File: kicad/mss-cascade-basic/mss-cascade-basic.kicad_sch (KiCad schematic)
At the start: 94 parts, among them J1 Screw_Terminal_01x02, J10 Screw_Terminal_01x02, J2 SM04B-SRSS, J3 SM04B-SRSS, J4 SM04B-SRSS, J5 8P8C, J6 8P8C, J7 AVR-ISP, J8 Screw_Terminal_01x02, J9 Screw_Terminal_01x02, U1 AP7381-50Y, U2 ATtiny861A-S, U3 74HC4049, U4 AP3012

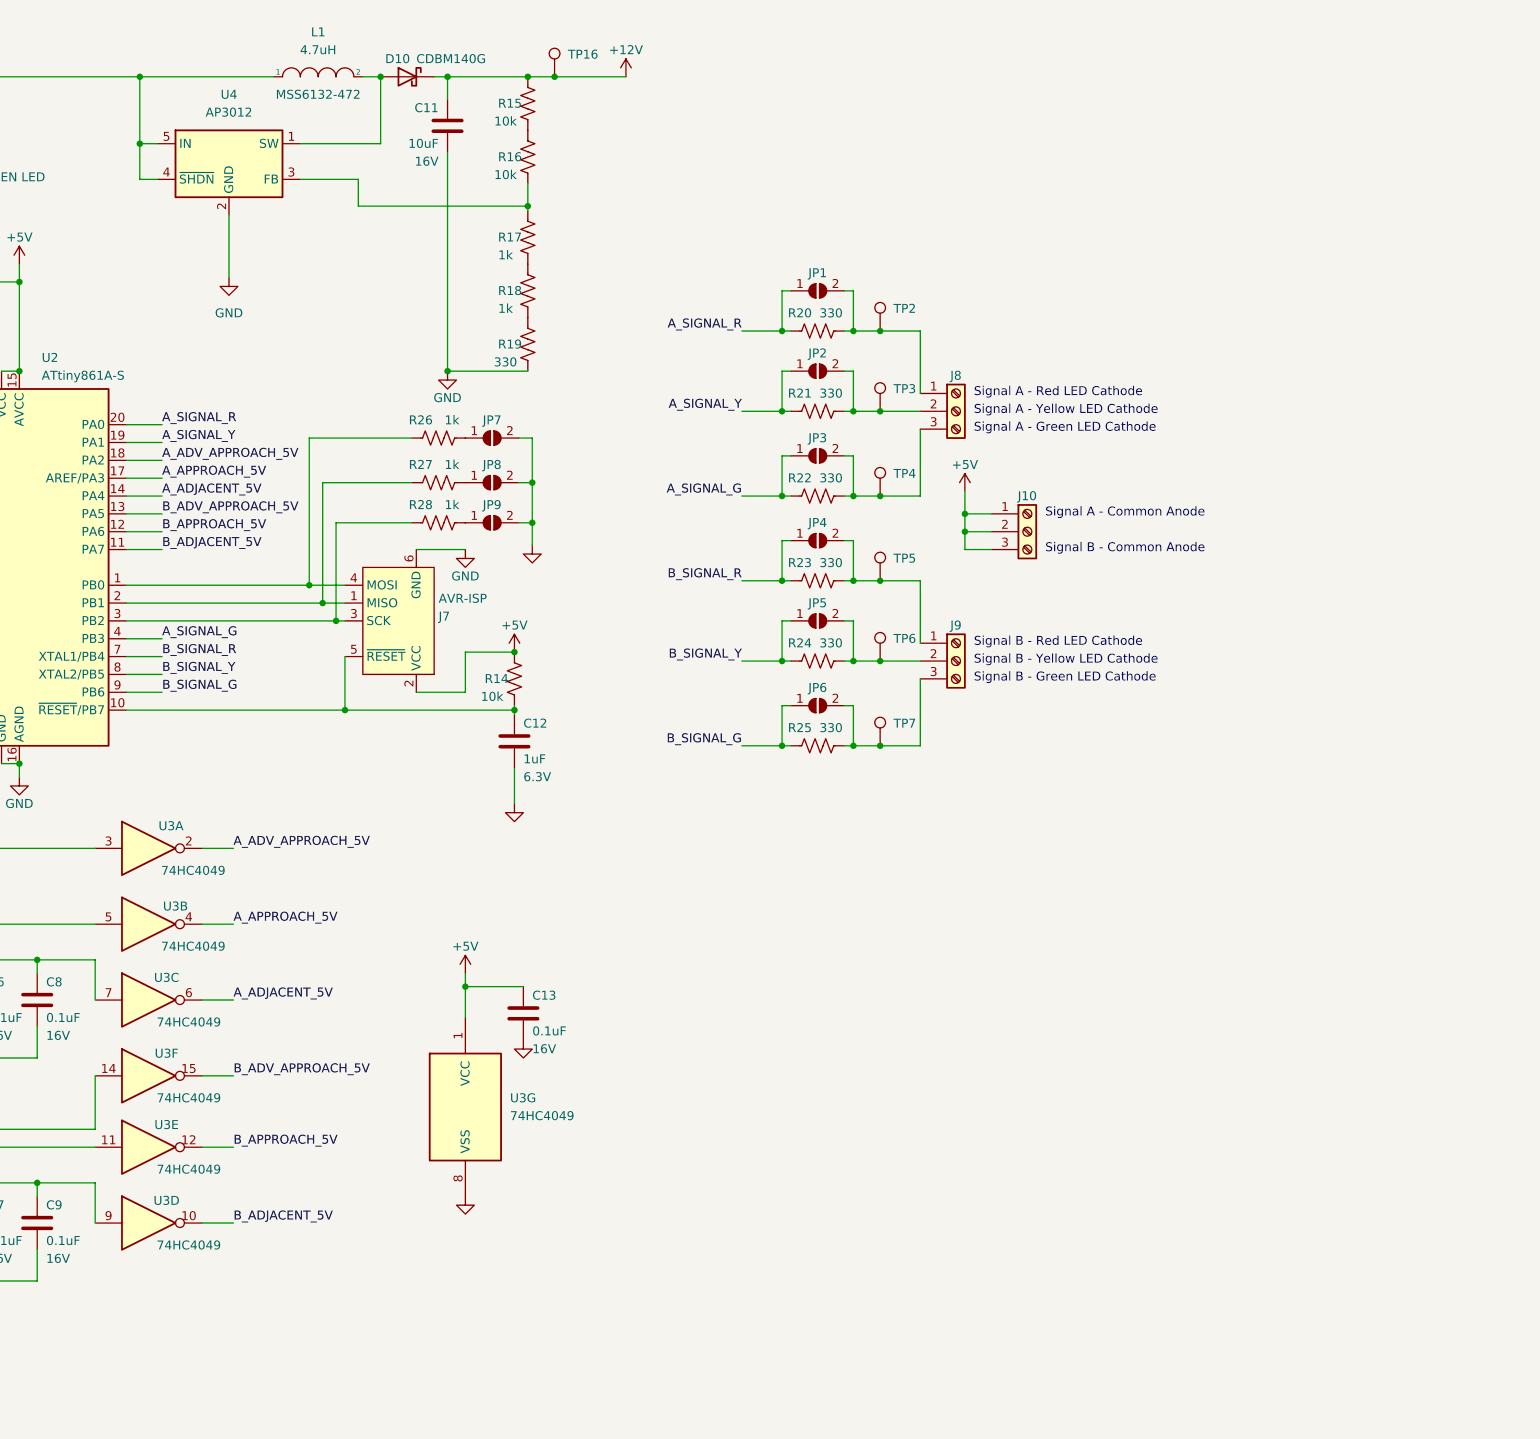
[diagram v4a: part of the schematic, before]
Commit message: Preliminary addition of Atlas signal connectors and the ability to set common anode or cathode
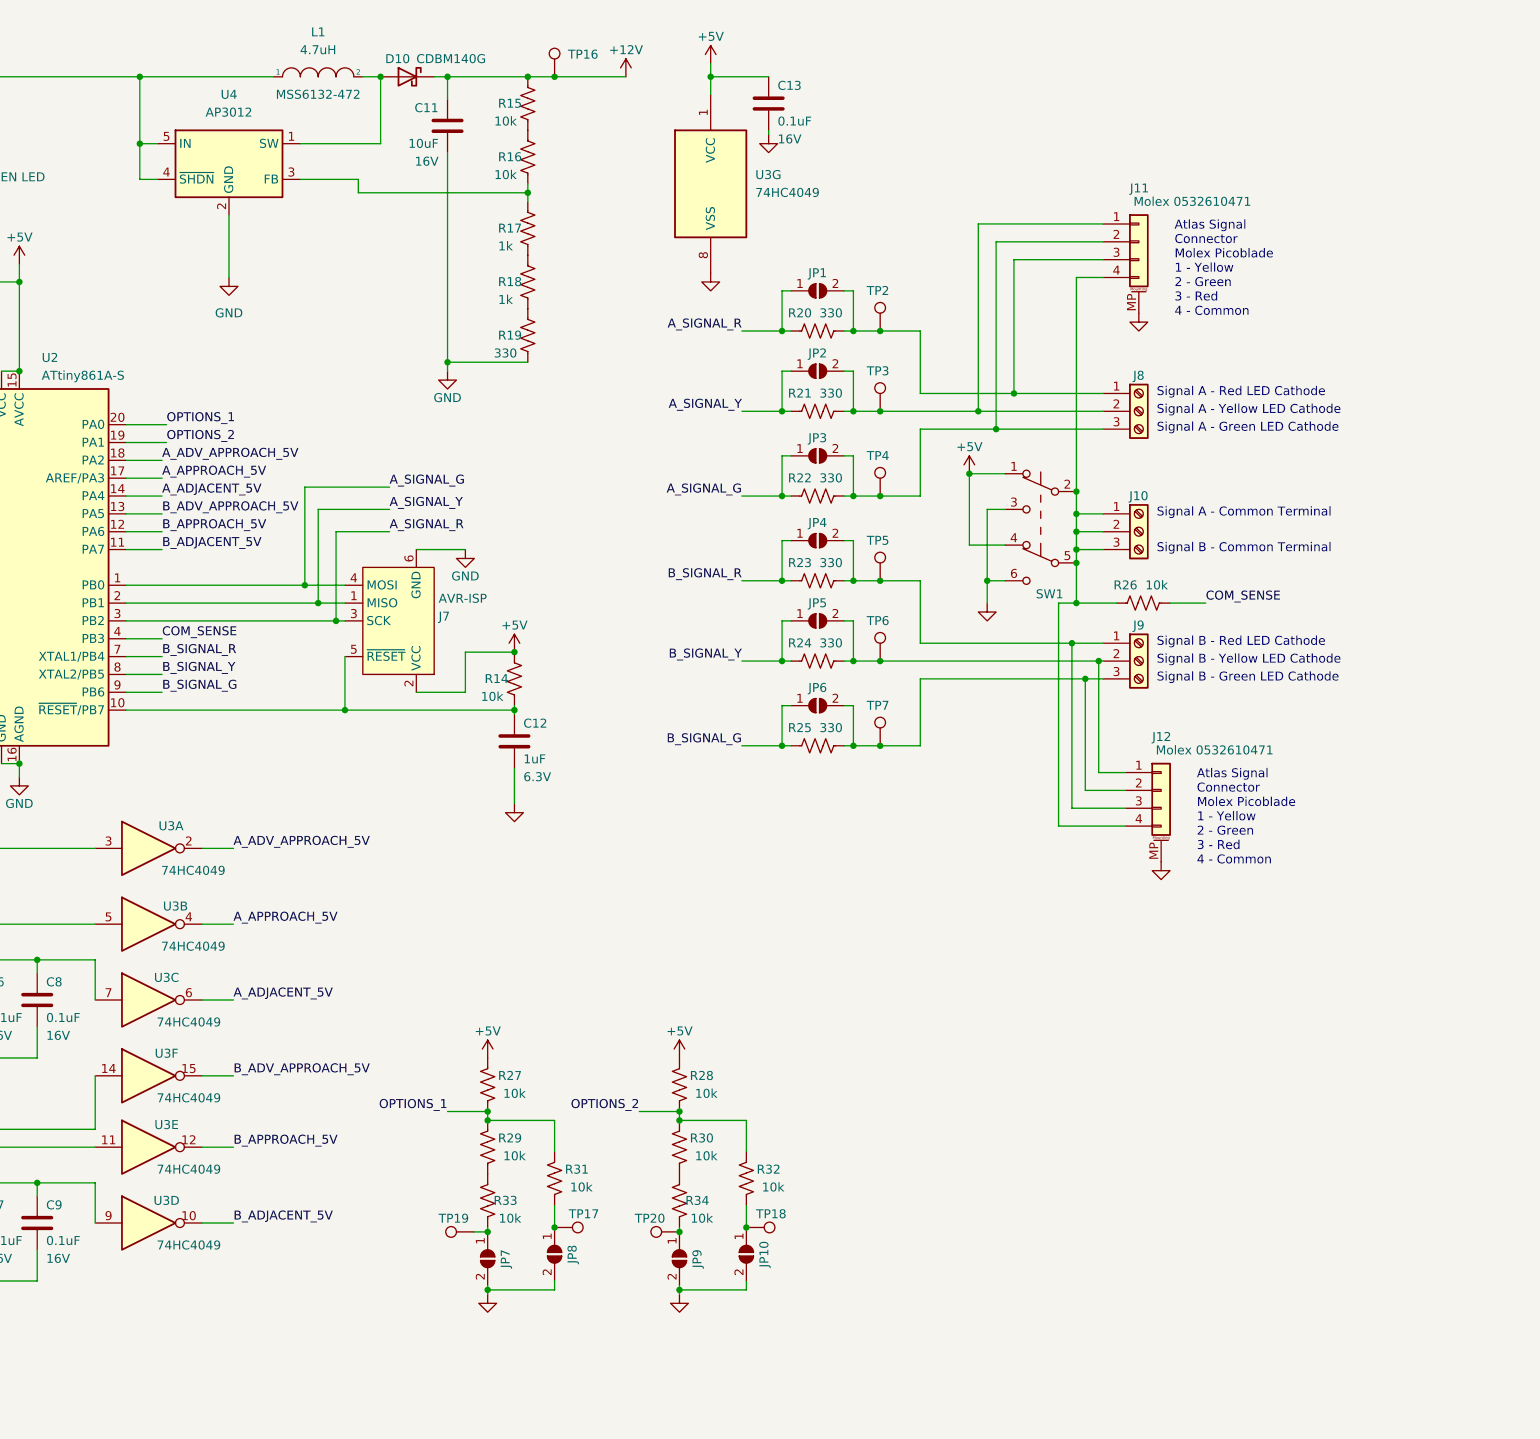
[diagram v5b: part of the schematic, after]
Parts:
- added J11, J12: Molex 0532610471, Connector_Molex:Molex_PicoBlade_53261-0471_1x04-1MP_P1.25mm_Horizontal, symbol Connector_Generic_MountingPin:Conn_01x04_MountingPin
- added JP10: SolderJumper_2_Open, Jumper:SolderJumper-2_P1.3mm_Open_RoundedPad1.0x1.5mm, symbol Jumper:SolderJumper_2_Open
- added R29, R30, R31, R32, R33, R34: 10k, Resistor_SMD:R_0805_2012Metric, symbol Device:R_US
- added SW1: JS202011SCQN, ISE_UltraLibrarian:SW_JS202011SCQN, symbol Switch:SW_Push_DPDT
- added TP17, TP18, TP19, TP20: TestPoint, TestPoint:TestPoint_Pad_D2.0mm, symbol Connector:TestPoint
- R26, R27, R28: value 1k -> 10k
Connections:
- net +5V: now also R27.2, R28.2, SW1.1 (A), SW1.4 (A); no longer J10.1 (Pin_1), J10.2 (Pin_2), J10.3 (Pin_3)
- net A_SIGNAL_G: now also J7.4 (MOSI), U2.1 (PB0); no longer U2.4 (PB3)
- net A_SIGNAL_R: now also J7.3 (SCK), U2.3 (PB2); no longer U2.20 (PA0)
- net A_SIGNAL_Y: now also J7.1 (MISO), U2.2 (PB1); no longer U2.19 (PA1)
- net GND: now also J11.MP (MountPin), J12.MP (MountPin), JP10.2 (B), SW1.3 (C), SW1.6 (C)
- net at JP9.1 (A): now also R34.1, TP20.1; no longer R28.2
- net at J9.2 (Pin_2), JP5.2 (B), R24.2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: now also J12.1 (Pin_1)
- net at J8.2 (Pin_2), JP2.2 (B), R21.2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: now also J11.1 (Pin_1)
- net at J9.1 (Pin_1), JP4.2 (B), R23.2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: now also J12.3 (Pin_3)
- net at J9.3 (Pin_3), JP6.2 (B), R25.2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: now also J12.2 (Pin_2)
- net at JP7.1 (A): now also R33.1, TP19.1; no longer R26.2
- net at J8.1 (Pin_1), JP1.2 (B), R20.2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: now also J11.3 (Pin_3)
- net at J8.3 (Pin_3), JP3.2 (B), R22.2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: now also J11.2 (Pin_2)
- net at JP8.1 (A): now also R31.1, TP17.1; no longer R27.2
- new net: J10.1 (Pin_1), J10.2 (Pin_2), J10.3 (Pin_3), J11.4 (Pin_4), J12.4 (Pin_4), R26.1, SW1.2 (B), SW1.5 (B)
- new net: R30.1, R34.2
- new net: R29.1, R33.2
- new net: JP10.1 (A), R32.1, TP18.1
- new net COM_SENSE: R26.2, U2.4 (PB3)
- new net OPTIONS_1: R27.1, R29.2, R31.2, U2.20 (PA0)
- new net OPTIONS_2: R28.1, R30.2, R32.2, U2.19 (PA1)
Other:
- note added: "Atlas Signal Connector Molex Picoblade 1 - Yellow 2 - Green 3 - Red 4 - Common"
- note added: "Signal A - Common Terminal"
- note added: "Signal B - Common Terminal"
- note removed: "Signal A - Common Anode"
- note removed: "Signal B - Common Anode"
- moved on the sheet: C13, J10, J8, J9, R17, R18, R19, U3G

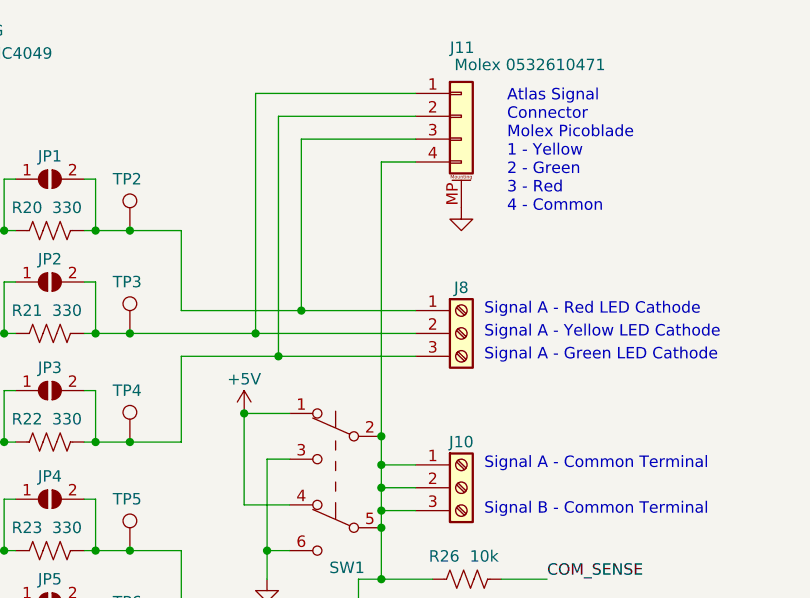
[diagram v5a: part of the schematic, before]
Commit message: Change text, add test point for common
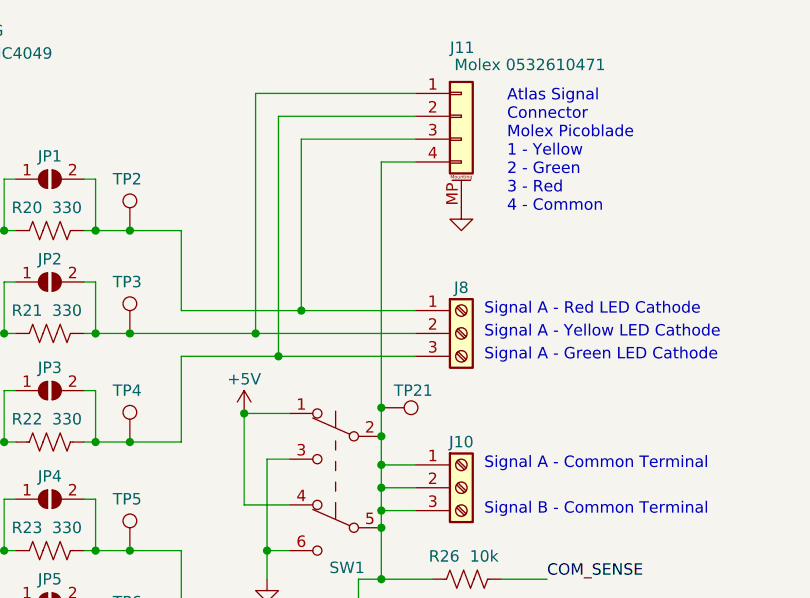
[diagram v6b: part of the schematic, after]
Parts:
- added TP21: TestPoint, TestPoint:TestPoint_Pad_D2.0mm, symbol Connector:TestPoint
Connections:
- net at J10.1 (Pin_1), J10.2 (Pin_2), J10.3 (Pin_3)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: now also TP21.1
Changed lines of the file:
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@@
   (junction (at 116.205 162.56) (diameter 0) (color 0 0 0 0)
   )
+  (junction (at 272.415 78.74) (diameter 0) (color 0 0 0 0)
+  )
   (junction (at 230.505 118.11) (diameter 0) (color 0 0 0 0)
   )
@@
     (stroke (width 0) (type default) (color 0 0 0 0))
   )
-  (wire (pts (xy 272.415 51.435) (xy 272.415 81.915))
+  (wire (pts (xy 272.415 51.435) (xy 272.415 78.74))
     (stroke (width 0) (type default) (color 0 0 0 0))
   )
@@
     (stroke (width 0) (type default) (color 0 0 0 0))
   )
+  (wire (pts (xy 272.415 78.74) (xy 272.415 81.915))
+    (stroke (width 0) (type default) (color 0 0 0 0))
+  )
   (wire (pts (xy 48.895 156.21) (xy 54.61 156.21))
     (stroke (width 0) (type default) (color 0 0 0 0))
@@
     (pin "2")
   )
+  (symbol (lib_id "Connector:TestPoint") (at 272.415 78.74 270) (mirror x) (unit 1)
+    (in_bom yes) (on_board yes)
+    (property "Reference" "TP21" (id 0) (at 278.13 76.835 90)
+      (effects (font (size 1.27 1.27)) (justify right))
+    )
+    (property "Value" "TestPoint" (id 1) (at 274.4471 76.835 0)
+      (effects (font (size 1.27 1.27)) (justify left) hide)
+    )
+    (property "Footprint" "TestPoint:TestPoint_Pad_D2.0mm" (id 2) (at 272.415 73.66 0)
+      (effects (font (size 1.27 1.27)) hide)
+    )
+    (property "Datasheet" "~" (id 3) (at 272.415 73.66 0)
+      (effects (font (size 1.27 1.27)) hide)
+    )
+    (pin "1")
+  )
   (symbol (lib_id "Device:R_US") (at 215.9 175.26 0) (mirror x) (unit 1)
     (in_bom yes) (on_board yes)
@@
       (reference "TP20") (unit 1) (value "TestPoint") (footprint "TestPoint:TestPoint_Pad_D2.0mm")
     )
+    (path "/6450e1ee-0a6f-4371-89d7-12a925669320"
+      (reference "TP21") (unit 1) (value "TestPoint") (footprint "TestPoint:TestPoint_Pad_D2.0mm")
+    )
     (path "/7a02355a-c87d-4d7e-9caa-076f50357812"
